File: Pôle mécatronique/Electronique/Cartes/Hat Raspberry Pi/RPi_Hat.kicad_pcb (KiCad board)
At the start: 2 copper layers, 65 x 59 mm, 31 parts, among them J1 Conn_02x03_Odd_Even, J2 RPi_GPIO, J3 Conn_01x02, U1 XBee, U2 MCP25625-x-SS, Y1 8MHz

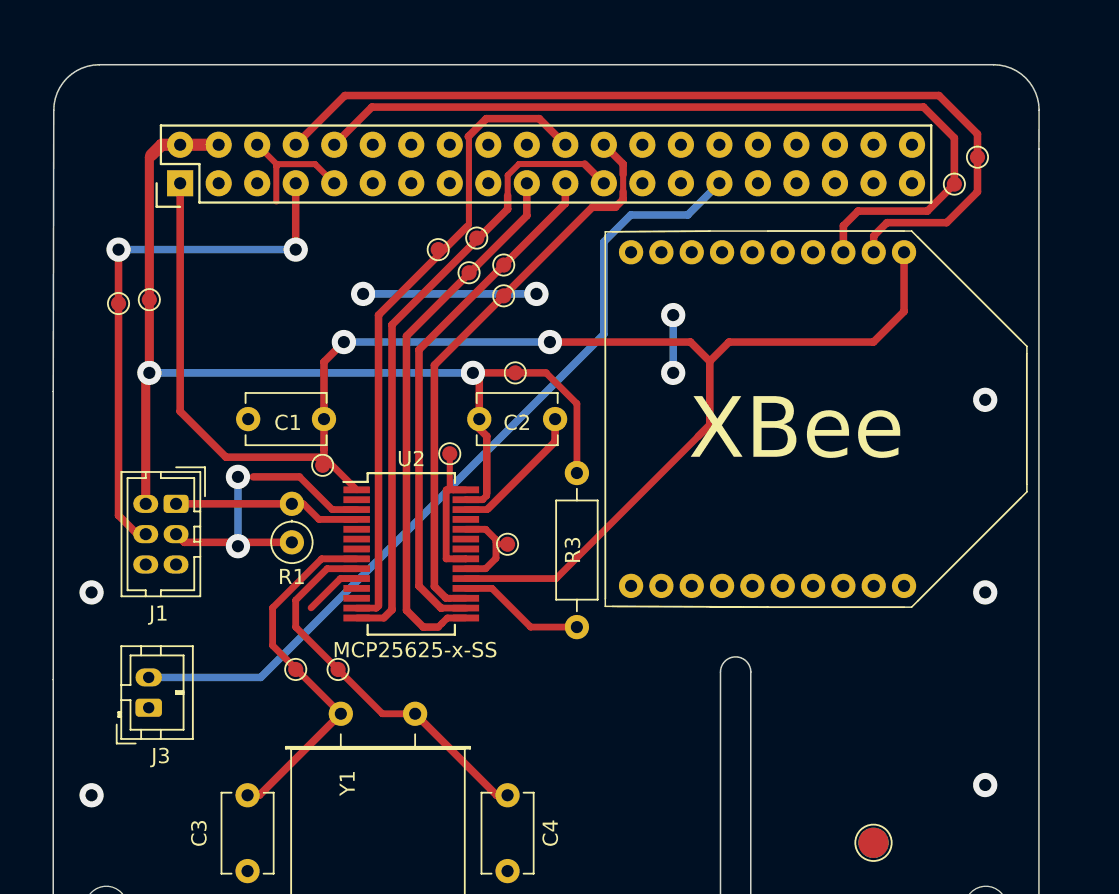
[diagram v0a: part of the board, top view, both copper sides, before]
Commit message: Update fabrication
Pistes et pastilles plus larges
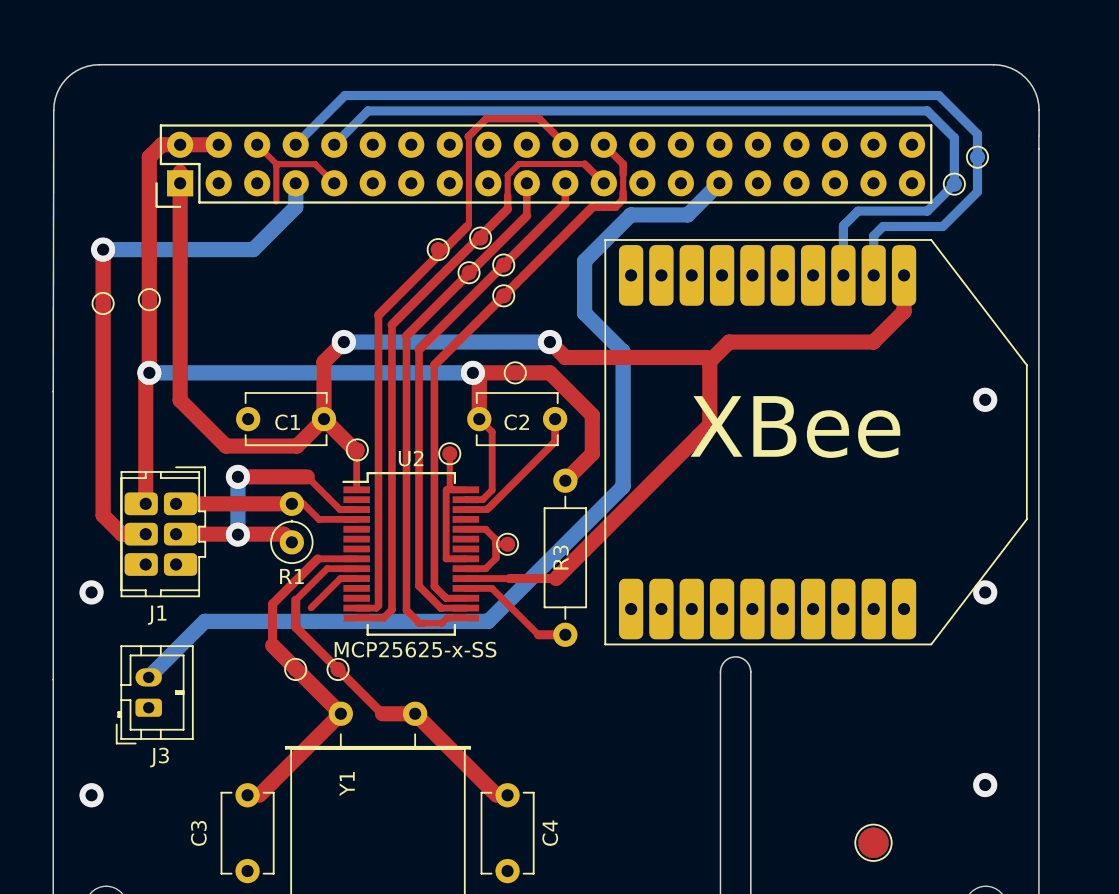
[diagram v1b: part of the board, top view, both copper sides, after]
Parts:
- moved REF** 2.50 mm to (80.3, 60.5)
- moved U1 1.52 mm to (107.3, 59.9)
- moved REF** 1.02 mm to (63.5, 50.8)
- moved R3 0.92 mm to (94.0, 62.5)
- moved REF** 0.25 mm to (88.4, 46.5)
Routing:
- net GND: track 39.7 -> 24.5 mm, vias 9 -> 5
- net /RPi_GPIO/Starter: track 54.7 -> 63.4 mm
- net +5V: track 71.4 -> 73.5 mm
- net +3.3VA: track 104.2 -> 104.9 mm
- net Net-(R3-Pad2): track 8.38 -> 7.83 mm
- net cmd_relais: track 35.9 -> 36.3 mm, vias 2 -> 1

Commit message: Update HAT
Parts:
- removed the REF** at (121.2, 41.1)
- removed the REF** at (119.6, 42.9)
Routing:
- net /RPi_GPIO/Starter: track 63.4 -> 69.9 mm, vias 0 -> 1
- net +3.3VA: track 104.9 -> 102.1 mm
- net /RPi_GPIO/BCM14_TXD: track 60.3 -> 62.4 mm, vias 0 -> 1
- net /RPi_GPIO/BCM15_RXD: track 55.8 -> 57.4 mm, vias 0 -> 1
- net +5V: track 73.5 -> 74.4 mm
- net cmd_relais: track 36.3 -> 36.9 mm, vias 1 -> 2
- net GND: vias 5 -> 4

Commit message: Update random
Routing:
- net INT: track 42.5 -> 43.1 mm
- net /RPi_GPIO/BCM14_TXD: track 62.4 -> 62.9 mm
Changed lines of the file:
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@@
     (fp_line (start -1.11 -2.11) (end -2.36 -2.11) (layer "F.Fab") (width 0.1))
     (fp_line (start 3.95 2.8) (end 3.95 -1.7) (layer "F.Fab") (width 0.1))
-    (pad "1" thru_hole roundrect locked (at 0 0 90) (size 1.2 1.75) (drill 0.75) (layers *.Cu *.Mask) (roundrect_rratio 0.2083333333)
+    (pad "1" thru_hole roundrect locked (at 0 0 90) (size 1.5 2) (drill 0.8) (layers *.Cu *.Mask) (roundrect_rratio 0.2083333333)
       (net 7 "GND") (pinfunction "Pin_1") (pintype "passive"))
-    (pad "2" thru_hole oval locked (at 2 0 90) (size 1.2 1.75) (drill 0.75) (layers *.Cu *.Mask)
+    (pad "2" thru_hole oval locked (at 2 0 90) (size 1.5 2) (drill 0.8) (layers *.Cu *.Mask)
       (net 24 "/RPi_GPIO/Starter") (pinfunction "Pin_2") (pintype "passive"))
     (model "${KICAD6_3DMODEL_DIR}/Connector_JST.3dshapes/JST_PH_B2B-PH-K_1x02_P2.00mm_Vertical.wrl"
@@
   (segment (start 81.519022 70.885) (end 81.661 70.743022) (width 0.45) (layer "F.Cu") (net 18))
   (segment (start 87.623111 45.599889) (end 87.503 45.72) (width 0.4) (layer "F.Cu") (net 18))
-  (segment (start 87.586889 39.786091) (end 87.586889 39.822313) (width 0.5) (layer "F.Cu") (net 18))
+  (segment (start 92.004 38.354) (end 88.392 38.354) (width 0.5) (layer "F.Cu") (net 18))
   (segment (start 80.22 70.885) (end 81.519022 70.885) (width 0.45) (layer "F.Cu") (net 18))
   (segment (start 81.661 51.562) (end 87.503 45.72) (width 0.6) (layer "F.Cu") (net 18))
   (segment (start 81.661 70.743022) (end 81.661 51.562) (width 0.5) (layer "F.Cu") (net 18))
-  (segment (start 93.98 40.33) (end 92.258 38.608) (width 0.5) (layer "F.Cu") (net 18))
-  (segment (start 88.76498 38.608) (end 87.586889 39.786091) (width 0.5) (layer "F.Cu") (net 18))
+  (segment (start 88.392 38.354) (end 87.586889 39.159111) (width 0.5) (layer "F.Cu") (net 18))
+  (segment (start 87.586889 39.159111) (end 87.586889 39.822313) (width 0.5) (layer "F.Cu") (net 18))
+  (segment (start 93.98 40.33) (end 92.004 38.354) (width 0.5) (layer "F.Cu") (net 18))
   (segment (start 87.623111 39.822313) (end 87.623111 45.599889) (width 0.4) (layer "F.Cu") (net 18))
-  (segment (start 92.258 38.608) (end 88.76498 38.608) (width 0.5) (layer "F.Cu") (net 18))
   (segment (start 80.22 71.535) (end 82.008 71.535) (width 0.45) (layer "F.Cu") (net 19))
   (segment (start 90.176889 44.570111) (end 90.176889 43.681111) (width 0.5) (layer "F.Cu") (net 19))
@@
   (segment (start 66.506 71.850924) (end 66.506 75.454) (width 1) (layer "B.Cu") (net 24))
   (segment (start 87.884 49.784) (end 66.548 49.784) (width 1) (layer "B.Cu") (net 24))
-  (segment (start 117.318489 37.054489) (end 122.428 42.164) (width 0.6) (layer "F.Cu") (net 33))
-  (segment (start 76.2 40.33) (end 76.2 38.862) (width 0.6) (layer "F.Cu") (net 33))
-  (segment (start 76.2 38.862) (end 78.007511 37.054489) (width 0.6) (layer "F.Cu") (net 33))
-  (segment (start 78.007511 37.054489) (end 117.318489 37.054489) (width 0.6) (layer "F.Cu") (net 33))
-  (via (at 122.428 42.164) (size 2) (drill 0.8) (layers "F.Cu" "B.Cu") (net 33))
+  (segment (start 78.007511 37.054489) (end 76.2 38.862) (width 0.6) (layer "F.Cu") (net 33))
+  (segment (start 76.2 38.862) (end 76.2 40.33) (width 0.6) (layer "F.Cu") (net 33))
+  (segment (start 118.969489 37.054489) (end 78.007511 37.054489) (width 0.6) (layer "F.Cu") (net 33))
+  (segment (start 121.92 40.005) (end 118.969489 37.054489) (width 0.6) (layer "F.Cu") (net 33))
+  (segment (start 121.92 42.164) (end 121.92 40.005) (width 0.6) (layer "F.Cu") (net 33))
+  (via (at 121.92 42.164) (size 2) (drill 0.8) (layers "F.Cu" "B.Cu") (net 33))
   (segment (start 114.315 46.34) (end 114.315 47.42) (width 0.6) (layer "B.Cu") (net 33))
-  (segment (start 122.428 42.164) (end 122.428 43.688) (width 0.6) (layer "B.Cu") (net 33))
+  (segment (start 120.396 45.72) (end 114.935 45.72) (width 0.6) (layer "B.Cu") (net 33))
   (segment (start 114.935 45.72) (end 114.315 46.34) (width 0.6) (layer "B.Cu") (net 33))
-  (segment (start 120.396 45.72) (end 114.935 45.72) (width 0.6) (layer "B.Cu") (net 33))
-  (segment (start 122.428 43.688) (end 120.396 45.72) (width 0.6) (layer "B.Cu") (net 33))
+  (segment (start 121.92 44.196) (end 120.396 45.72) (width 0.6) (layer "B.Cu") (net 33))
+  (segment (start 121.92 42.164) (end 121.92 44.196) (width 0.6) (layer "B.Cu") (net 33))
   (segment (start 79.502 38.354) (end 78.74 39.116) (width 0.6) (layer "F.Cu") (net 34))
   (segment (start 80.01 38.354) (end 79.502 38.354) (width 0.6) (layer "F.Cu") (net 34))
@@
         (xy 65.405 62.865)
         (xy 64.135 62.865)
-        (xy 64.77 46.355)
-        (xy 65.405 46.355)
+        (xy 64.643 45.72)
+        (xy 65.786 45.339)
       )
     )
@@
     (polygon
       (pts
-        (xy 154.94 116.205)
-        (xy 41.275 114.935)
-        (xy 41.275 21.59)
-        (xy 154.305 20.955)
+        (xy 126.365 95.25)
+        (xy 59.055 95.25)
+        (xy 59.055 33.655)
+        (xy 125.73 33.655)
       )
     )
@@
     (polygon
       (pts
-        (xy 162.306 115.57)
-        (xy 39.116 115.062)
-        (xy 38.608 26.67)
-        (xy 160.02 23.876)
+        (xy 126.365 95.25)
+        (xy 59.055 95.25)
+        (xy 59.055 33.655)
+        (xy 125.74221 33.655117)
       )
     )

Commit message: Update BR
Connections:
- U1 pad 2: /RPi_GPIO/BCM14_TXD -> /RPi_GPIO/BCM15_RXD
- U1 pad 3: /RPi_GPIO/BCM15_RXD -> /RPi_GPIO/BCM14_TXD
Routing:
- net /RPi_GPIO/BCM15_RXD: track 57.4 -> 60.2 mm
- net /RPi_GPIO/BCM14_TXD: track 62.9 -> 60.6 mm
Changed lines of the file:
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@@
       (net 69 "+3.3VA") (pinfunction "VCC") (pintype "input"))
     (pad "2" thru_hole roundrect (at -11 -7 270) (size 4 1.6) (drill 0.8) (layers *.Cu *.Mask) (roundrect_rratio 0.25)
-      (net 33 "/RPi_GPIO/BCM14_TXD") (pinfunction "DOUT") (pintype "output"))
+      (net 34 "/RPi_GPIO/BCM15_RXD") (pinfunction "DOUT") (pintype "output"))
     (pad "3" thru_hole roundrect (at -11 -5 270) (size 4 1.6) (drill 0.8) (layers *.Cu *.Mask) (roundrect_rratio 0.25)
-      (net 34 "/RPi_GPIO/BCM15_RXD") (pinfunction "DIN") (pintype "input"))
+      (net 33 "/RPi_GPIO/BCM14_TXD") (pinfunction "DIN") (pintype "input"))
     (pad "4" thru_hole roundrect (at -11 -3 270) (size 4 1.6) (drill 0.8) (layers *.Cu *.Mask) (roundrect_rratio 0.25)
       (net 35 "unconnected-(U1-Pad4)") (pinfunction "DIO12") (pintype "bidirectional+no_connect"))
@@
   (segment (start 66.506 71.850924) (end 66.506 75.454) (width 1) (layer "B.Cu") (net 24))
   (segment (start 87.884 49.784) (end 66.548 49.784) (width 1) (layer "B.Cu") (net 24))
-  (segment (start 78.007511 37.054489) (end 76.2 38.862) (width 0.6) (layer "F.Cu") (net 33))
-  (segment (start 76.2 38.862) (end 76.2 40.33) (width 0.6) (layer "F.Cu") (net 33))
-  (segment (start 118.969489 37.054489) (end 78.007511 37.054489) (width 0.6) (layer "F.Cu") (net 33))
-  (segment (start 121.92 40.005) (end 118.969489 37.054489) (width 0.6) (layer "F.Cu") (net 33))
-  (segment (start 121.92 42.164) (end 121.92 40.005) (width 0.6) (layer "F.Cu") (net 33))
-  (via (at 121.92 42.164) (size 2) (drill 0.8) (layers "F.Cu" "B.Cu") (net 33))
-  (segment (start 114.315 46.34) (end 114.315 47.42) (width 0.6) (layer "B.Cu") (net 33))
-  (segment (start 120.396 45.72) (end 114.935 45.72) (width 0.6) (layer "B.Cu") (net 33))
-  (segment (start 114.935 45.72) (end 114.315 46.34) (width 0.6) (layer "B.Cu") (net 33))
-  (segment (start 121.92 44.196) (end 120.396 45.72) (width 0.6) (layer "B.Cu") (net 33))
-  (segment (start 121.92 42.164) (end 121.92 44.196) (width 0.6) (layer "B.Cu") (net 33))
-  (segment (start 79.502 38.354) (end 78.74 39.116) (width 0.6) (layer "F.Cu") (net 34))
-  (segment (start 80.01 38.354) (end 79.502 38.354) (width 0.6) (layer "F.Cu") (net 34))
-  (segment (start 78.74 39.116) (end 78.74 40.33) (width 0.6) (layer "F.Cu") (net 34))
-  (via (at 80.01 38.354) (size 1.6) (drill 0.8) (layers "F.Cu" "B.Cu") (net 34))
-  (segment (start 80.01 38.354) (end 80.018581 38.345419) (width 0.6) (layer "B.Cu") (net 34))
-  (segment (start 119.888 40.132) (end 119.888 44.196) (width 0.6) (layer "B.Cu") (net 34))
-  (segment (start 113.284 44.704) (end 112.315 45.673) (width 0.6) (layer "B.Cu") (net 34))
-  (segment (start 80.018581 38.345419) (end 118.101419 38.345419) (width 0.6) (layer "B.Cu") (net 34))
-  (segment (start 118.101419 38.345419) (end 119.888 40.132) (width 0.6) (layer "B.Cu") (net 34))
-  (segment (start 119.38 44.704) (end 113.284 44.704) (width 0.6) (layer "B.Cu") (net 34))
-  (segment (start 112.315 45.673) (end 112.315 47.42) (width 0.6) (layer "B.Cu") (net 34))
-  (segment (start 119.888 44.196) (end 119.38 44.704) (width 0.6) (layer "B.Cu") (net 34))
+  (segment (start 76.2 38.1) (end 76.2 40.33) (width 1) (layer "F.Cu") (net 33))
+  (via (at 76.2 38.1) (size 1.6) (drill 0.8) (layers "F.Cu" "B.Cu") (net 33))
+  (segment (start 118.872 44.704) (end 113.284 44.704) (width 0.6) (layer "B.Cu") (net 33))
+  (segment (start 113.284 44.704) (end 112.315 45.673) (width 0.6) (layer "B.Cu") (net 33))
+  (segment (start 119.38 39.624) (end 117.221 37.465) (width 1) (layer "B.Cu") (net 33))
+  (segment (start 112.315 45.673) (end 112.315 47.42) (width 0.6) (layer "B.Cu") (net 33))
+  (segment (start 117.221 37.465) (end 76.835 37.465) (width 1) (layer "B.Cu") (net 33))
+  (segment (start 119.38 44.196) (end 118.872 44.704) (width 0.6) (layer "B.Cu") (net 33))
+  (segment (start 119.38 44.196) (end 119.38 39.624) (width 1) (layer "B.Cu") (net 33))
+  (segment (start 76.835 37.465) (end 76.2 38.1) (width 1) (layer "B.Cu") (net 33))
+  (segment (start 80.137 37.338) (end 78.74 38.735) (width 0.6) (layer "F.Cu") (net 34))
+  (segment (start 121.92 42.164) (end 121.92 40.005) (width 0.6) (layer "F.Cu") (net 34))
+  (segment (start 119.253 37.338) (end 80.137 37.338) (width 0.6) (layer "F.Cu") (net 34))
+  (segment (start 121.92 40.005) (end 119.253 37.338) (width 0.6) (layer "F.Cu") (net 34))
+  (segment (start 78.74 38.735) (end 78.74 40.33) (width 0.6) (layer "F.Cu") (net 34))
+  (via (at 121.92 42.164) (size 2) (drill 0.8) (layers "F.Cu" "B.Cu") (net 34))
+  (segment (start 114.315 46.34) (end 114.315 47.42) (width 0.6) (layer "B.Cu") (net 34))
+  (segment (start 120.396 45.72) (end 114.935 45.72) (width 0.6) (layer "B.Cu") (net 34))
+  (segment (start 114.935 45.72) (end 114.315 46.34) (width 0.6) (layer "B.Cu") (net 34))
+  (segment (start 121.92 44.196) (end 120.396 45.72) (width 0.6) (layer "B.Cu") (net 34))
+  (segment (start 121.92 42.164) (end 121.92 44.196) (width 0.6) (layer "B.Cu") (net 34))
   (segment (start 73.801 83.225) (end 73.025 83.225) (width 0.6) (layer "F.Cu") (net 55))
   (segment (start 79.175 77.851) (end 73.801 83.225) (width 1) (layer "F.Cu") (net 55))
